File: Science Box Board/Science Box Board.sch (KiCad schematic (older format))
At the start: 40 parts, among them U1 Molex_SL-2, U10 LB1930MC, U11 Molex_SL-10, U12 Molex_SL_2, U13 Molex_SL_5, U2 Molex_SL-2, U3 5V OKI, U4 OPA320, U5 OPA320, U6 5V OKI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

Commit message: Finalized board and generated gerbs
Changed name of board from "Science Signals Booster" to "Science Box Board". Board Review for Rev 1, generated Gerbs
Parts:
- U1, U2: symbol Molex_SL-2 -> Molex_SL_2
- U11: symbol Molex_SL-10 -> Molex_SL_10
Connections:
- wire segments 125 -> 119
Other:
- note removed: "Need TIVA pins selected for IN1, IN2\n(This implementation is based on last years\nboard which connected to the same motor)"
- note removed: "Need TIVA pins selected for magINC, magDEC"
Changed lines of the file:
@@
 LIBS:MRDT_Silkscreens
 LIBS:MRDT_Switches
-LIBS:Science Signals Booster-cache
 EELAYER 25 0
 EELAYER END
@@
 Laser Control
 $Comp
-L Molex_SL-10 U11
+L Molex_SL_10 U11
 U 1 1 5AA82860
-P 14100 4200
-F 0 "U11" H 14150 4150 60  0001 C CNN
-F 1 "Molex_SL-10" H 14300 4750 60  0000 C CNN
-F 2 "MRDT_Connectors:MOLEX_SL_10_Horizontal" H 14100 4200 60  0001 C CNN
-F 3 "" H 14100 4200 60  0001 C CNN
-	1    14100 4200
+P 14100 4700
+F 0 "U11" H 14150 4650 60  0001 C CNN
+F 1 "Molex_SL-10" H 14300 5250 60  0000 C CNN
+F 2 "MRDT_Connectors:MOLEX_SL_10_Horizontal" H 14100 4700 60  0001 C CNN
+F 3 "" H 14100 4700 60  0001 C CNN
+	1    14100 4700
 	1    0    0    -1
 $EndComp
@@
 Text Notes 2550 1700 0    98   ~ 0
 Power
-$Comp
-L GND #PWR01
-U 1 1 5AB05B69
-P 3300 3150
-F 0 "#PWR01" H 3300 2900 50  0001 C CNN
-F 1 "GND" H 3300 3000 50  0000 C CNN
-F 2 "" H 3300 3150 50  0001 C CNN
-F 3 "" H 3300 3150 50  0001 C CNN
-	1    3300 3150
-	1    0    0    -1
-$EndComp
 Text GLabel 4600 2050 0    49   Input ~ 0
 LOGIC-12V
@@
 ACT-12V
 $Comp
-L GND #PWR02
+L GND #PWR01
 U 1 1 5AB1C63A
 P 4750 1850
-F 0 "#PWR02" H 4750 1600 50  0001 C CNN
+F 0 "#PWR01" H 4750 1600 50  0001 C CNN
 F 1 "GND" H 4750 1700 50  0000 C CNN
 F 2 "" H 4750 1850 50  0001 C CNN
@@
 	1    0    0    -1
 $EndComp
-$Comp
-L GND #PWR03
-U 1 1 5AB1DACF
-P 5700 3150
-F 0 "#PWR03" H 5700 2900 50  0001 C CNN
-F 1 "GND" H 5700 3000 50  0000 C CNN
-F 2 "" H 5700 3150 50  0001 C CNN
-F 3 "" H 5700 3150 50  0001 C CNN
-	1    5700 3150
-	1    0    0    -1
-$EndComp
 Text GLabel 5850 2750 0    49   Input ~ 0
 ACT-12V
@@
 $EndComp
 $Comp
-L Molex_SL-2 U1
+L Molex_SL_2 U1
 U 1 1 5AB1FE22
 P 3400 5150
@@
 	1    3400 5150
 	-1   0    0    1
-$EndComp
-$Comp
-L GND #PWR04
-U 1 1 5AB1FECA
-P 3700 5350
-F 0 "#PWR04" H 3700 5100 50  0001 C CNN
-F 1 "GND" H 3700 5200 50  0000 C CNN
-F 2 "" H 3700 5350 50  0001 C CNN
-F 3 "" H 3700 5350 50  0001 C CNN
-	1    3700 5350
-	1    0    0    -1
 $EndComp
 Text GLabel 3550 4600 0    49   Input ~ 0
@@
 Text GLabel 5000 4650 1    49   Input ~ 0
 LOGIC-5V
-$Comp
-L GND #PWR05
-U 1 1 5AB21586
-P 5400 5650
-F 0 "#PWR05" H 5400 5400 50  0001 C CNN
-F 1 "GND" H 5400 5500 50  0000 C CNN
-F 2 "" H 5400 5650 50  0001 C CNN
-F 3 "" H 5400 5650 50  0001 C CNN
-	1    5400 5650
-	1    0    0    -1
-$EndComp
 Text GLabel 6250 7600 2    49   Output ~ 0
 PHOTODIODE_2
@@
 $EndComp
 $Comp
-L Molex_SL-2 U2
+L Molex_SL_2 U2
 U 1 1 5AB21C1D
 P 3450 7650
@@
 	1    3450 7650
 	-1   0    0    1
-$EndComp
-$Comp
-L GND #PWR06
-U 1 1 5AB21C23
-P 3750 7850
-F 0 "#PWR06" H 3750 7600 50  0001 C CNN
-F 1 "GND" H 3750 7700 50  0000 C CNN
-F 2 "" H 3750 7850 50  0001 C CNN
-F 3 "" H 3750 7850 50  0001 C CNN
-	1    3750 7850
-	1    0    0    -1
 $EndComp
 Text GLabel 3600 7100 0    49   Input ~ 0
@@
 Text GLabel 5050 7150 1    49   Input ~ 0
 LOGIC-5V
-$Comp
-L GND #PWR07
-U 1 1 5AB21C78
-P 5450 8150
-F 0 "#PWR07" H 5450 7900 50  0001 C CNN
-F 1 "GND" H 5450 8000 50  0000 C CNN
-F 2 "" H 5450 8150 50  0001 C CNN
-F 3 "" H 5450 8150 50  0001 C CNN
-	1    5450 8150
-	1    0    0    -1
-$EndComp
 Text GLabel 8800 7800 0    49   Input ~ 0
 ACT-12V
@@
 Text Notes 12250 1700 0    98   ~ 0
 Spectrometer Motor
-Text Notes 12300 2750 0    39   ~ 0
-Need TIVA pins selected for IN1, IN2\n(This implementation is based on last years\nboard which connected to the same motor)
 Wire Wire Line
 	8400 5150 8600 5150
@@
 	4750 1800 4850 1800
 Connection ~ 3600 2750
-Wire Wire Line
-	3300 3100 3300 3150
 Wire Wire Line
 	3950 2750 3950 3000
@@
 Connection ~ 6000 2750
 Wire Wire Line
-	5700 3100 5700 3150
-Wire Wire Line
 	6350 2750 6350 3000
 Wire Wire Line
@@
 Wire Wire Line
 	3600 5300 3700 5300
-Wire Wire Line
-	3700 5300 3700 5350
 Wire Wire Line
 	3600 5200 4550 5200
@@
 	5450 4750 5450 5600
 Wire Wire Line
-	5450 5600 4750 5600
+	4750 5600 5700 5600
 Wire Wire Line
 	4750 5600 4750 5400
-Wire Wire Line
-	5400 5600 5400 5650
-Connection ~ 5400 5600
 Wire Wire Line
 	4750 4750 4750 4800
@@
 Wire Wire Line
 	3650 7800 3750 7800
-Wire Wire Line
-	3750 7800 3750 7850
 Wire Wire Line
 	3650 7700 4600 7700
@@
 	5500 7250 5500 8100
 Wire Wire Line
-	5500 8100 4800 8100
+	4800 8100 5750 8100
 Wire Wire Line
 	4800 8100 4800 7900
-Wire Wire Line
-	5450 8100 5450 8150
-Connection ~ 5450 8100
 Wire Wire Line
 	4800 7250 4800 7300
@@
 Wire Notes Line
 	12200 3100 15150 3100
-Text Notes 12800 5950 0    39   ~ 0
-Need TIVA pins selected for magINC, magDEC
 Wire Notes Line
 	12200 5300 15150 5300
@@
 Text GLabel 10450 8800 3    60   UnSpc ~ 0
 GND
+Text GLabel 3300 3100 0    60   UnSpc ~ 0
+GND
+Text GLabel 5700 3100 0    60   UnSpc ~ 0
+GND
+Text GLabel 3700 5300 2    60   UnSpc ~ 0
+GND
+Text GLabel 3750 7800 2    60   UnSpc ~ 0
+GND
+Connection ~ 5500 8100
+Text GLabel 5750 8100 2    60   UnSpc ~ 0
+GND
+Connection ~ 5450 5600
+Text GLabel 5700 5600 2    60   UnSpc ~ 0
+GND
+Text GLabel 8600 5550 0    60   Output ~ 0
++3V3
+Text GLabel 9500 5550 2    49   Output ~ 0
+LOGIC-5V
 $EndSCHEMATC

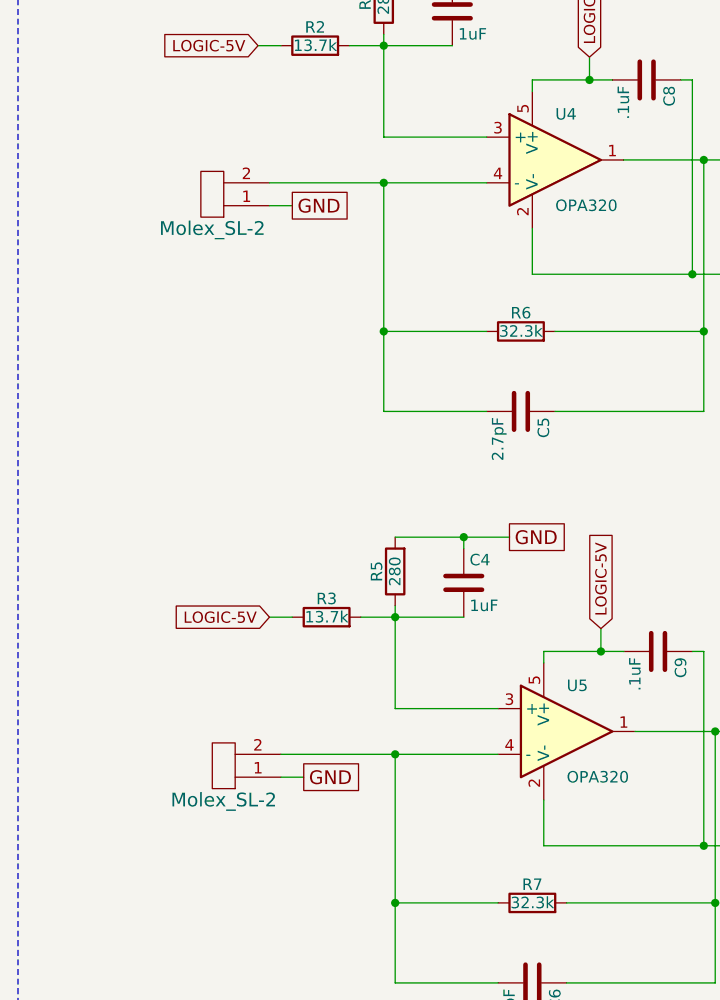
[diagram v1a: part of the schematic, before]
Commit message: Changed Molex SL2 to SL3 for photodiode connections and added 3v3 to them
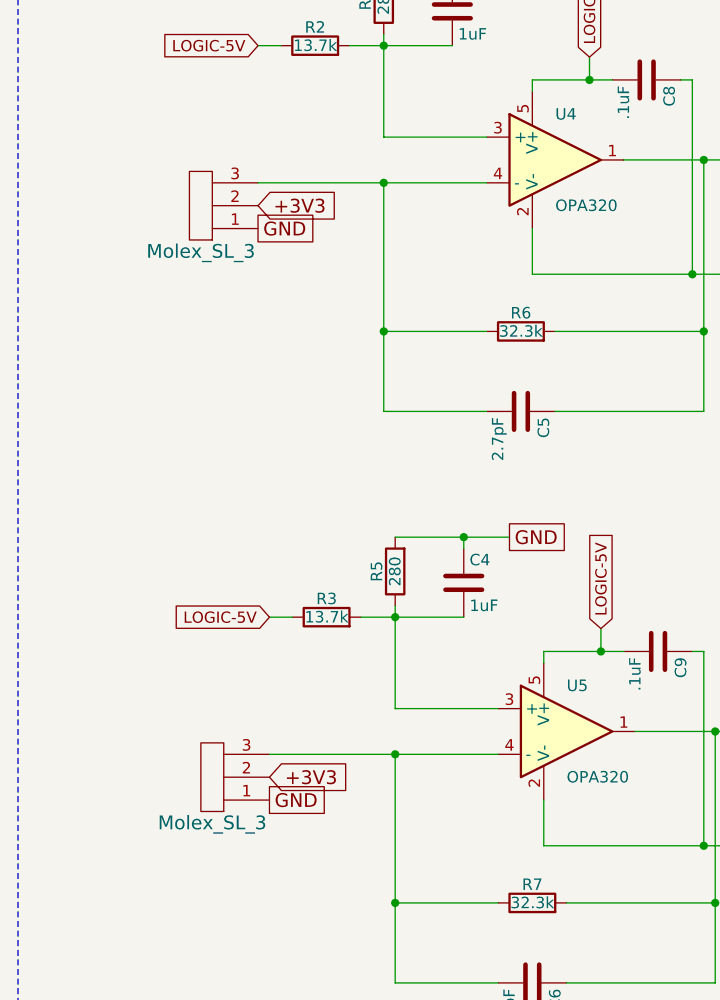
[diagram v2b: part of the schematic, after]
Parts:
- removed U1, U2: Molex_SL-2, MRDT_Connectors:MOLEX_SL_2_Horizontal, symbol Molex_SL_2
- added Conn? (x2): Molex_SL_3, symbol Molex_SL_3
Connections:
- net +3V3: now also Conn?.2, Conn?.2
- net GND: now also Conn?.1, Conn?.1
- net at C5.2, R6.1, U4.4 (-): now also Conn?.3
- net at C6.2, R7.1, U5.4 (-): now also Conn?.3
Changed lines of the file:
@@
 LIBS:MRDT_Silkscreens
 LIBS:MRDT_Switches
+LIBS:Science Box Board-cache
 EELAYER 25 0
 EELAYER END
@@
 	1    0    0    -1
 $EndComp
-$Comp
-L Molex_SL_2 U1
-U 1 1 5AB1FE22
-P 3400 5150
-F 0 "U1" H 3450 5100 60  0001 C CNN
-F 1 "Molex_SL-2" H 3450 5400 60  0000 C CNN
-F 2 "MRDT_Connectors:MOLEX_SL_2_Horizontal" H 3400 5050 60  0001 C CNN
-F 3 "" H 3400 5050 60  0001 C CNN
-	1    3400 5150
-	-1   0    0    1
-$EndComp
 Text GLabel 3550 4600 0    49   Input ~ 0
 LOGIC-5V
@@
 	1    0    0    -1
 $EndComp
-$Comp
-L Molex_SL_2 U2
-U 1 1 5AB21C1D
-P 3450 7650
-F 0 "U2" H 3500 7600 60  0001 C CNN
-F 1 "Molex_SL-2" H 3500 7900 60  0000 C CNN
-F 2 "MRDT_Connectors:MOLEX_SL_2_Horizontal" H 3450 7550 60  0001 C CNN
-F 3 "" H 3450 7550 60  0001 C CNN
-	1    3450 7650
-	-1   0    0    1
-$EndComp
 Text GLabel 3600 7100 0    49   Input ~ 0
 LOGIC-5V
@@
 	2500 4150 7150 4150
 Wire Wire Line
-	3600 5300 3700 5300
-Wire Wire Line
-	3600 5200 4550 5200
+	3550 5200 4550 5200
 Wire Wire Line
 	3550 4600 3650 4600
@@
 Connection ~ 5000 4750
 Wire Wire Line
-	3650 7800 3750 7800
-Wire Wire Line
-	3650 7700 4600 7700
+	3600 7700 4600 7700
 Wire Wire Line
 	3600 7100 3700 7100
@@
 Text GLabel 5700 3100 0    60   UnSpc ~ 0
 GND
-Text GLabel 3700 5300 2    60   UnSpc ~ 0
-GND
-Text GLabel 3750 7800 2    60   UnSpc ~ 0
+Text GLabel 3550 5400 2    60   UnSpc ~ 0
+GND
+Text GLabel 3600 7900 2    60   UnSpc ~ 0
 GND
 Connection ~ 5500 8100
@@
 Text GLabel 9500 5550 2    49   Output ~ 0
 LOGIC-5V
+$Comp
+L Molex_SL_3 Conn?
+U 1 1 5AD94F0D
+P 3350 5150
+F 0 "Conn?" H 3400 5100 60  0001 C CNN
+F 1 "Molex_SL_3" H 3400 5500 60  0000 C CNN
+F 2 "" H 3350 5150 60  0001 C CNN
+F 3 "" H 3350 5150 60  0001 C CNN
+	1    3350 5150
+	-1   0    0    1
+$EndComp
+Text GLabel 3550 5300 2    60   Input ~ 0
++3V3
+Text GLabel 3600 7800 2    60   Input ~ 0
++3V3
+$Comp
+L Molex_SL_3 Conn?
+U 1 1 5AD9540E
+P 3400 7650
+F 0 "Conn?" H 3450 7600 60  0001 C CNN
+F 1 "Molex_SL_3" H 3450 8000 60  0000 C CNN
+F 2 "" H 3400 7650 60  0001 C CNN
+F 3 "" H 3400 7650 60  0001 C CNN
+	1    3400 7650
+	-1   0    0    1
+$EndComp
 $EndSCHEMATC
